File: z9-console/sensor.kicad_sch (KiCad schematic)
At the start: 17 parts, among them Q1 AO3400A, U4 ST_SENSOR_2, U5 IIS3DHHCTR

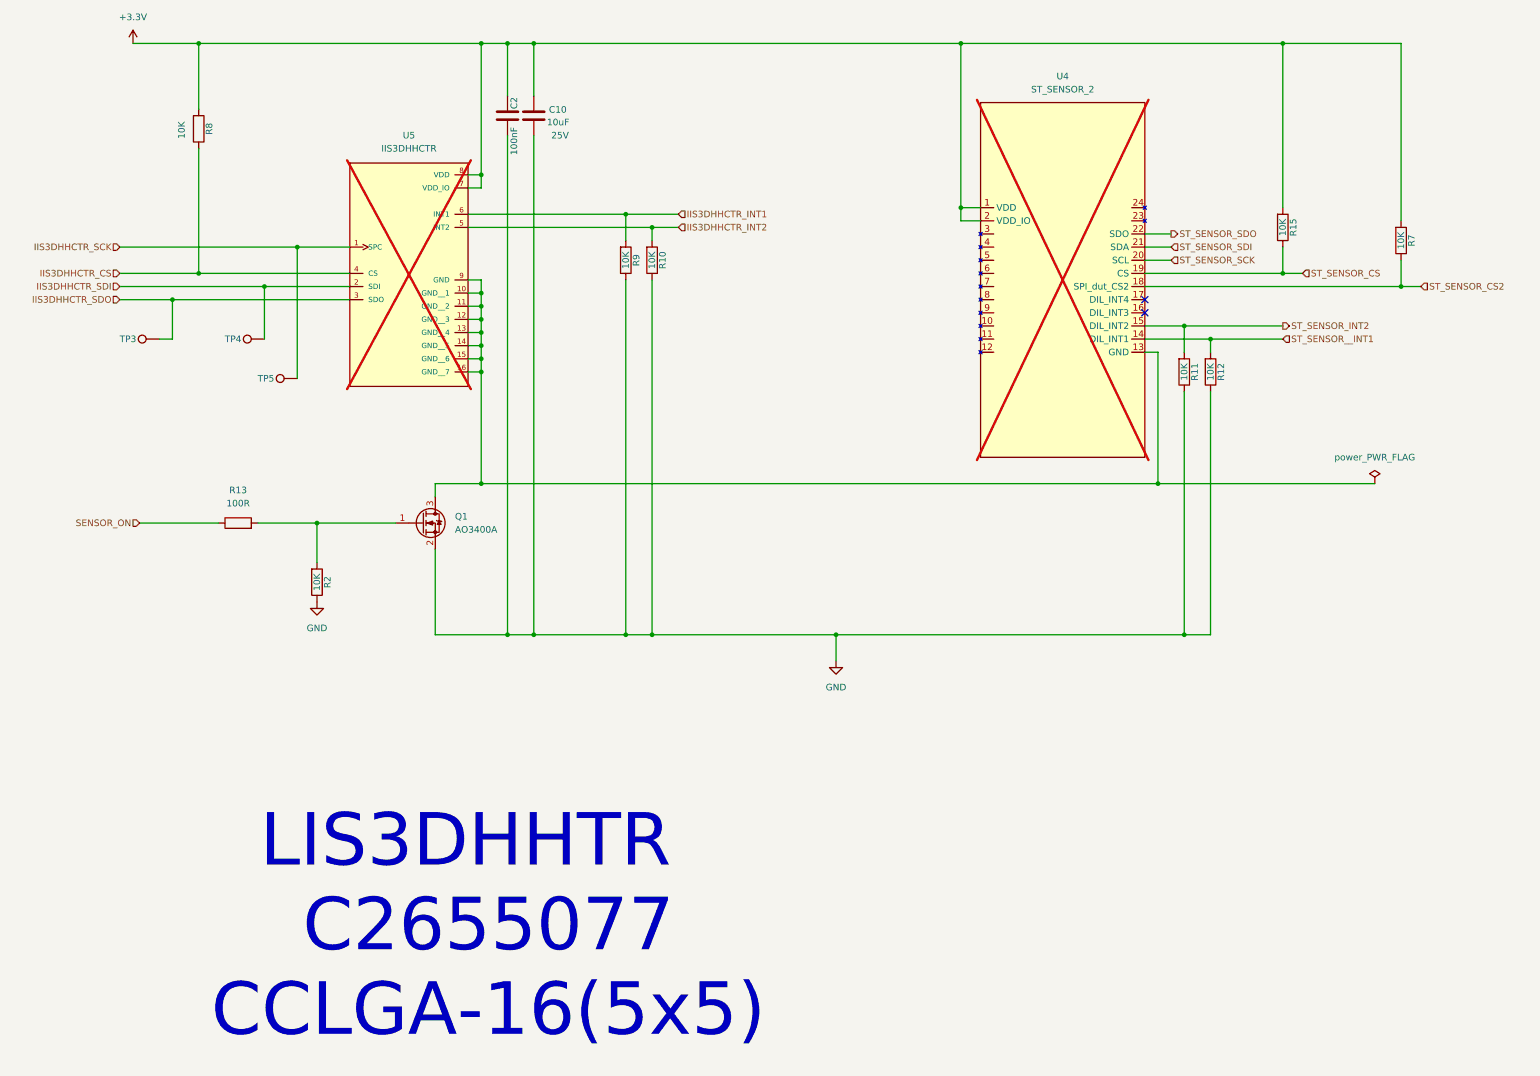
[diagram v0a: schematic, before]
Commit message: lcd power switch-- add new accelerometer
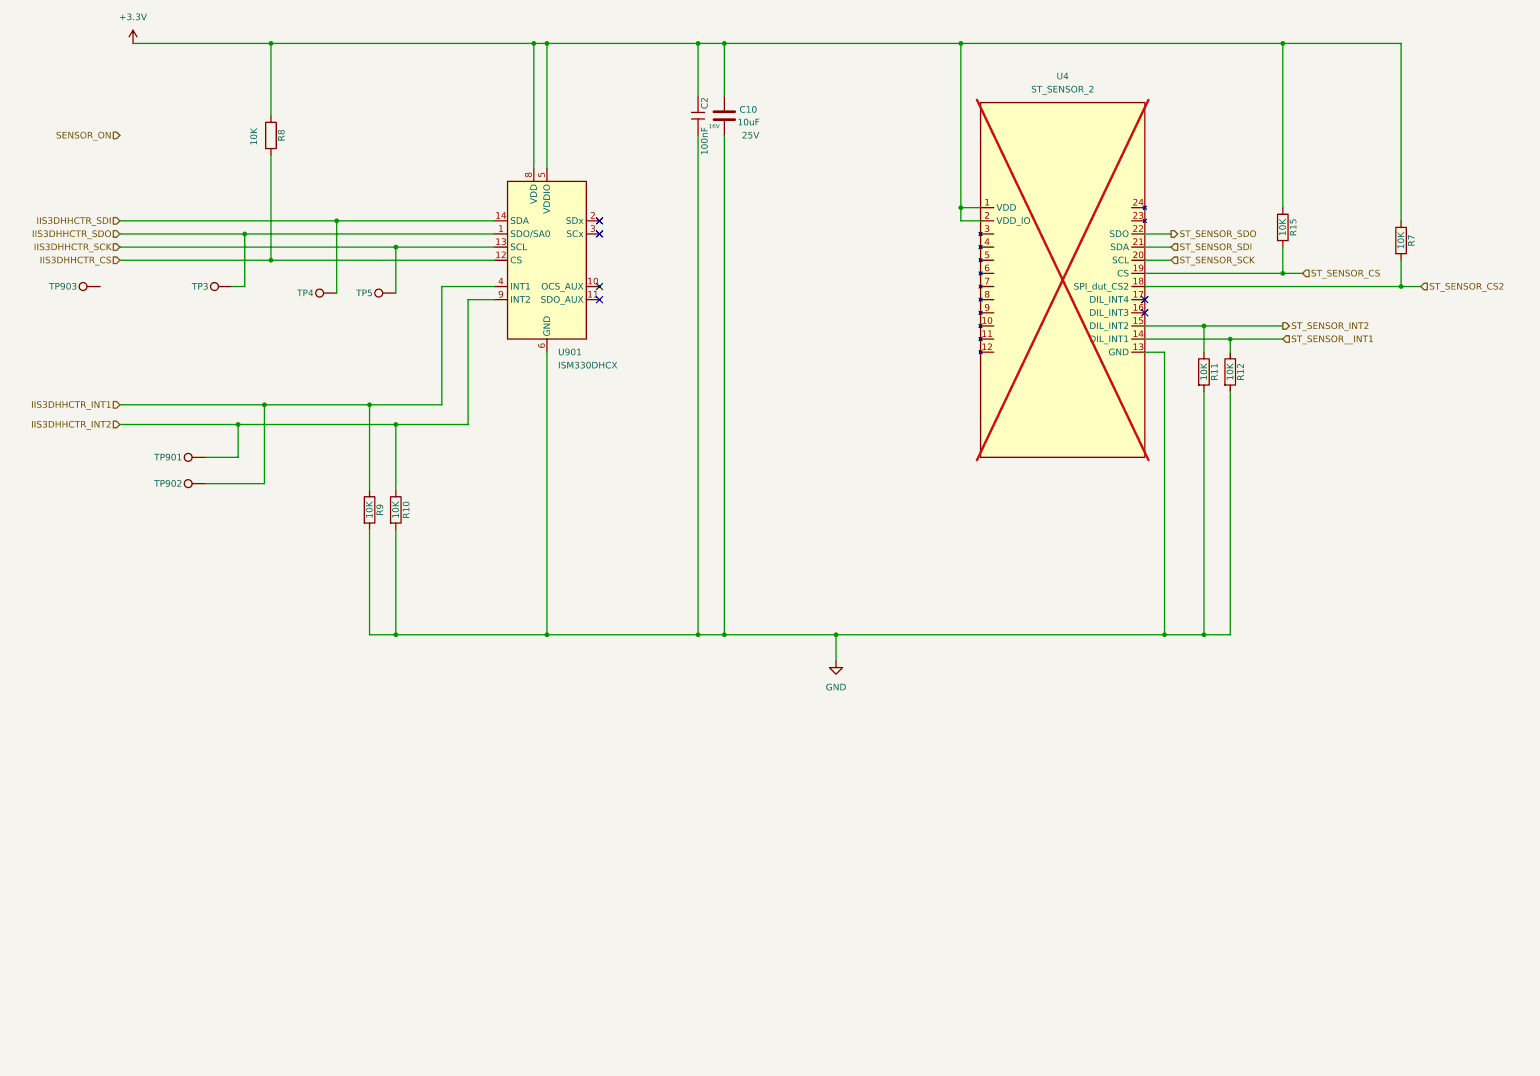
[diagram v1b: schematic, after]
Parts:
- removed Q1: AO3400A, Package_TO_SOT_SMD:SOT-23, symbol dnt_global:AO3400A
- removed R13: 100R, Resistor_SMD:R_0603_1608Metric, symbol Device:R
- removed R2: 10K, Resistor_SMD:R_0603_1608Metric, symbol Device:R
- removed U5: IIS3DHHCTR, dnt:CCLGA-16L_5X5X1P7_STM, symbol dnt_global:IIS3DHHCTR
- added TP901, TP902, TP903: IIS3DHHCTR_SDI, dnt:TestPoint_Pad_D1.0mm FP .6R, symbol Connector:TestPoint
- added U901: ISM330DHCX, Package_LGA:LGA-14_3x2.5mm_P0.5mm_LayoutBorder3x4y, symbol dnt_global:ISM330DHCX
- C2: footprint Capacitor_SMD:C_0603_1608Metric -> PCM_JLCPCB:C_0402; symbol Device:C -> dnt_global:0402,100nF, 16V; Attrition Qty (none) -> 10; Capacitance (none) -> 100nF; Category (none) -> Capacitors,Multilayer Ceramic Capacitors MLCC - SMD/SMT; Class (none) -> Basic Component; LCSC C14663 -> C1525; Manufacturer (none) -> Samsung Electro-Mechanics; Minimum Qty (none) -> 20; Part (none) -> CL05B104KO5NNNC; Price (none) -> 0.004USD; Process (none) -> SMT; Stock (none) -> 20208285; Temperature Coefficient (none) -> X7R; Tolerance (none) -> ±10%; Voltage Rated (none) -> 16V
- R10, R9: footprint Resistor_SMD:R_0603_1608Metric -> PCM_JLCPCB:R_0402; symbol Device:R -> dnt_global:Resistor_0402,10kΩ; Attrition Qty (none) -> 10; Category (none) -> Resistors,Chip Resistor - Surface Mount; Class (none) -> Basic Component; LCSC C25804 -> C25744; Manufacturer StackPole -> UNI-ROYAL(Uniroyal Elec); Minimum Qty (none) -> 20; Operating Temperature Range (none) -> -55°C~+155°C; Overload Voltage (Max) (none) -> 50V; Part (none) -> 0402WGF1002TCE; Part # RMCF0603JT10K0 -> (none); Power(Watts) (none) -> 62.5mW; Price (none) -> 0.004USD; Process (none) -> SMT; Resistance (none) -> 10kΩ; Stock (none) -> 24372091; Temperature Coefficient (none) -> ±100ppm/°C; Tolerance (none) -> ±1%; Type (none) -> Thick Film Resistors; VEND DIGI -> (none); VEND# RMCF0603JT10K0CT-ND -> (none)
- R11, R12, R15, R7, R8: footprint Resistor_SMD:R_0603_1608Metric -> PCM_JLCPCB:R_0402; symbol Device:R -> dnt_global:Resistor_0402,10kΩ; Attrition Qty (none) -> 10; Category (none) -> Resistors,Chip Resistor - Surface Mount; Class (none) -> Basic Component; LCSC C25804 -> C25744; Manufacturer (none) -> UNI-ROYAL(Uniroyal Elec); Minimum Qty (none) -> 20; Operating Temperature Range (none) -> -55°C~+155°C; Overload Voltage (Max) (none) -> 50V; Part (none) -> 0402WGF1002TCE; Power(Watts) (none) -> 62.5mW; Price (none) -> 0.004USD; Process (none) -> SMT; Resistance (none) -> 10kΩ; Stock (none) -> 24372091; Temperature Coefficient (none) -> ±100ppm/°C; Tolerance (none) -> ±1%; Type (none) -> Thick Film Resistors
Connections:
- net +3.3V: now also U901.5 (VDDIO), U901.8 (VDD)
- net GND: now also U4.13 (GND), U901.6 (GND), U901.7 (GND)
- net IIS3DHHCTR_CS: now also U901.12 (CS)
- net IIS3DHHCTR_INT1: now also TP902.1, U901.4 (INT1)
- net IIS3DHHCTR_INT2: now also TP901.1, U901.9 (INT2)
- net IIS3DHHCTR_SCK: now also U901.13 (SCL)
- net IIS3DHHCTR_SDI: now also U901.14 (SDA)
- net IIS3DHHCTR_SDO: now also U901.1 (SDO/SA0)
- no-connect marks 2 -> 6
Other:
- note removed: "LIS3DHHTR C2655077 CCLGA-16(5x5)"
- moved on the sheet: C10, C2, R10, R11, R12, R8, R9, TP3, TP4, TP5

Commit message: change MEMS device
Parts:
- renumbered C2 to C28, C10 to C29, R8 to R21, R9 to R22, R10 to R23, R11 to R24, R12 to R25, R15 to R26, R7 to R27, TP903 to TP37, TP901 to TP38, TP902 to TP39, TP3 to TP40, TP4 to TP41, TP5 to TP42, U901 to U10, U4 to U11
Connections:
- net IIS3DHHCTR_CS: now also TP37.1
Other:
- moved on the sheet: TP37, TP41, TP42

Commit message: final lcsc mappings
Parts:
- U10: LCSC (none) -> C2655101
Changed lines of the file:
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@@
 	(wire
 		(pts
-			(xy 245.11 78.74) (xy 260.35 78.74)
+			(xy 245.11 78.74) (xy 287.02 78.74)
 		)
 		(stroke
@@
 	(wire
 		(pts
-			(xy 260.35 68.58) (xy 264.16 68.58)
+			(xy 260.35 68.58) (xy 287.02 68.58)
 		)
 		(stroke
@@
 	(wire
 		(pts
-			(xy 250.19 81.28) (xy 260.35 81.28)
+			(xy 250.19 81.28) (xy 287.02 81.28)
 		)
 		(stroke
@@
 	(hierarchical_label "ST_SENSOR_CS"
 		(shape input)
-		(at 264.16 68.58 0)
+		(at 287.02 68.58 0)
 		(effects
 			(font
@@
 	(hierarchical_label "ST_SENSOR_INT2"
 		(shape output)
-		(at 260.35 78.74 0)
+		(at 287.02 78.74 0)
 		(effects
 			(font
@@
 	(hierarchical_label "ST_SENSOR__INT1"
 		(shape input)
-		(at 260.35 81.28 0)
+		(at 287.02 81.28 0)
 		(effects
 			(font
@@
 			(effects
 				(font
+					(size 1.27 1.27)
+				)
+				(hide yes)
+			)
+		)
+		(property "LCSC" " C2655101"
+			(at 118.11 66.04 0)
+			(effects
+				(font

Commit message: fix stdc - reroute power on pcb
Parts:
- TP37: value IIS3DHHCTR_SDI -> ISM_CS
- TP38: value IIS3DHHCTR_SDI -> ISM_INT1
- TP39: value IIS3DHHCTR_SDI -> ISM_INT2
- TP40: value IIS3DHHCTR_SDI -> ISM_SDO
- TP41: value IIS3DHHCTR_SDI -> ISM_SDI
- TP42: value IIS3DHHCTR_SCK -> ISM3_SCK
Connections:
- net +3.3V: now also U10.11 (SDO_AUX), U10.2 (SDx), U10.3 (SCx)
- net IIS3DHHCTR_CS renamed ISM_CS
- net IIS3DHHCTR_INT1 renamed ISM_INT1
- net IIS3DHHCTR_INT2 renamed ISM_INT2
- net IIS3DHHCTR_SCK renamed ISM_SCK
- net IIS3DHHCTR_SDI renamed ISM_SDI
- net IIS3DHHCTR_SDO renamed ISM_SDO
- no-connect marks 6 -> 3
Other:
- moved on the sheet: TP40
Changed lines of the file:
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@@
 	(paper "A3")
 	(junction
+		(at 132.08 58.42)
+		(diameter 0)
+		(color 0 0 0 0)
+	)
+	(junction
 		(at 147.32 138.43)
 		(diameter 0)
@@
 	)
 	(junction
+		(at 132.08 24.13)
+		(diameter 0)
+		(color 0 0 0 0)
+	)
+	(junction
 		(at 115.57 24.13)
 		(diameter 0)
@@
 	)
 	(junction
+		(at 132.08 60.96)
+		(diameter 0)
+		(color 0 0 0 0)
+	)
+	(junction
 		(at 198.12 55.88)
 		(diameter 0)
@@
 	)
 	(no_connect
-		(at 128.27 73.66)
-	)
-	(no_connect
-		(at 128.27 60.96)
-	)
-	(no_connect
-		(at 128.27 58.42)
-	)
-	(no_connect
 		(at 233.68 73.66)
 	)
@@
 	(wire
 		(pts
+			(xy 132.08 24.13) (xy 147.32 24.13)
+		)
+		(stroke
+			(width 0)
+			(type default)
+		)
+	)
+	(wire
+		(pts
 			(xy 260.35 24.13) (xy 283.21 24.13)
 		)
@@
 	(wire
 		(pts
+			(xy 128.27 58.42) (xy 132.08 58.42)
+		)
+		(stroke
+			(width 0)
+			(type default)
+		)
+	)
+	(wire
+		(pts
 			(xy 97.79 71.12) (xy 97.79 93.98)
 		)
@@
 	(wire
 		(pts
-			(xy 59.69 71.12) (xy 59.69 60.96)
+			(xy 59.69 72.39) (xy 59.69 60.96)
 		)
 		(stroke
@@
 	(wire
 		(pts
+			(xy 132.08 60.96) (xy 132.08 58.42)
+		)
+		(stroke
+			(width 0)
+			(type default)
+		)
+	)
+	(wire
+		(pts
 			(xy 63.5 109.22) (xy 63.5 93.98)
 		)
@@
 	(wire
 		(pts
-			(xy 57.15 71.12) (xy 59.69 71.12)
+			(xy 58.42 72.39) (xy 59.69 72.39)
 		)
 		(stroke
@@
 	(wire
 		(pts
+			(xy 128.27 60.96) (xy 132.08 60.96)
+		)
+		(stroke
+			(width 0)
+			(type default)
+		)
+	)
+	(wire
+		(pts
+			(xy 128.27 73.66) (xy 132.08 73.66)
+		)
+		(stroke
+			(width 0)
+			(type default)
+		)
+	)
+	(wire
+		(pts
 			(xy 233.68 78.74) (xy 245.11 78.74)
 		)
@@
 	(wire
 		(pts
-			(xy 118.11 24.13) (xy 147.32 24.13)
+			(xy 118.11 24.13) (xy 132.08 24.13)
 		)
 		(stroke
@@
 	(wire
 		(pts
+			(xy 132.08 58.42) (xy 132.08 24.13)
+		)
+		(stroke
+			(width 0)
+			(type default)
+		)
+	)
+	(wire
+		(pts
 			(xy 173.99 138.43) (xy 237.49 138.43)
 		)
@@
 	(wire
 		(pts
+			(xy 132.08 73.66) (xy 132.08 60.96)
+		)
+		(stroke
+			(width 0)
+			(type default)
+		)
+	)
+	(wire
+		(pts
 			(xy 152.4 24.13) (xy 198.12 24.13)
 		)
@@
 		)
 	)
-	(hierarchical_label "IIS3DHHCTR_SDO"
+	(hierarchical_label "ISM_SDO"
 		(shape input)
 		(at 35.56 60.96 180)
@@
 		)
 	)
-	(hierarchical_label "IIS3DHHCTR_INT1"
+	(hierarchical_label "ISM_INT1"
 		(shape input)
 		(at 35.56 93.98 180)
@@
 		)
 	)
-	(hierarchical_label "IIS3DHHCTR_SCK"
+	(hierarchical_label "ISM_SCK"
 		(shape input)
 		(at 35.56 63.5 180)
@@
 		)
 	)
-	(hierarchical_label "IIS3DHHCTR_INT2"
+	(hierarchical_label "ISM_INT2"
 		(shape input)
 		(at 35.56 97.79 180)
@@
 		)
 	)
-	(hierarchical_label "IIS3DHHCTR_SDI"
+	(hierarchical_label "ISM_SDI"
 		(shape input)
 		(at 35.56 58.42 180)
@@
 		)
 	)
-	(hierarchical_label "IIS3DHHCTR_CS"
+	(hierarchical_label "ISM_CS"
 		(shape input)
 		(at 35.56 66.04 180)
@@
 			)
 		)
-		(property "Value" "IIS3DHHCTR_SDI"
+		(property "Value" "ISM_INT2"
 			(at 42.545 109.22 90)
 			(effects
@@
 				)
 				(justify left)
-				(hide yes)
 			)
 		)
@@
 		(dnp no)
 		(property "Reference" "TP37"
-			(at 80.645 72.39 90)
+			(at 82.804 70.358 90)
 			(effects
 				(font
@@
 			)
 		)
-		(property "Value" "IIS3DHHCTR_SDI"
-			(at 75.565 72.39 90)
+		(property "Value" "ISM_CS"
+			(at 82.55 74.676 90)
 			(effects
 				(font
@@
 				)
 				(justify left)
-				(hide yes)
 			)
 		)
@@
 	(symbol
 		(lib_id "Connector:TestPoint")
-		(at 57.15 71.12 90)
+		(at 58.42 72.39 90)
 		(unit 1)
 		(exclude_from_sim no)
@@
 		(dnp no)
 		(property "Reference" "TP40"
-			(at 52.705 71.12 90)
+			(at 57.404 70.612 90)
 			(effects
 				(font
@@
 			)
 		)
-		(property "Value" "IIS3DHHCTR_SDI"
-			(at 47.625 71.12 90)
+		(property "Value" "ISM_SDO"
+			(at 58.928 75.184 90)
 			(effects
 				(font
@@
 				)
 				(justify left)
-				(hide yes)
 			)
 		)
 		(property "Footprint" "dnt:TestPoint_Pad_D1.0mm FP .6R"
-			(at 57.15 66.04 0)
+			(at 58.42 67.31 0)
 			(effects
 				(font
@@
 		)
 		(property "Datasheet" "~"
-			(at 57.15 66.04 0)
+			(at 58.42 67.31 0)
 			(effects
 				(font
@@
 		)
 		(property "Description" "test point"
-			(at 57.15 71.12 0)
+			(at 58.42 72.39 0)
 			(effects
 				(font
@@
 		)
 		(property "Part #" "DNP"
-			(at 202.565 285.75 0)
+			(at 203.835 287.02 0)
 			(effects
 				(font
@@
 		)
 		(property "VEND" "DNP"
-			(at 202.565 285.75 0)
+			(at 203.835 287.02 0)
 			(effects
 				(font
@@
 		)
 		(property "VEND#" "DNP"
-			(at 202.565 285.75 0)
+			(at 203.835 287.02 0)
 			(effects
 				(font
@@
 		)
 		(property "Manufacturer" "DNP"
-			(at 202.565 285.75 0)
+			(at 203.835 287.02 0)
 			(effects
 				(font
@@
 		)
 		(property "Sim.Device" ""
-			(at 57.15 71.12 0)
+			(at 58.42 72.39 0)
 			(effects
 				(font
@@
 		)
 		(property "Sim.Pins" ""
-			(at 57.15 71.12 0)
+			(at 58.42 72.39 0)
 			(effects
 				(font
@@
 		)
 		(property "Silkscreen" ""
-			(at 57.15 71.12 0)
+			(at 58.42 72.39 0)
 			(effects
 				(font
@@
 		(dnp no)
 		(property "Reference" "TP42"
-			(at 66.675 72.39 90)
+			(at 69.596 70.612 90)
 			(effects
 				(font
@@
 			)
 		)
-		(property "Value" "IIS3DHHCTR_SCK"
-			(at 61.595 72.39 90)
+		(property "Value" "ISM3_SCK"
+			(at 72.136 74.93 90)
 			(effects
 				(font
@@
 				)
 				(justify left)
-				(hide yes)
 			)
 		)
@@
 			)
 		)
-		(property "Value" "IIS3DHHCTR_SDI"
+		(property "Value" "ISM_INT1"
 			(at 42.545 104.14 90)
 			(effects
@@
 				)
 				(justify left)
-				(hide yes)
 			)
 		)
@@
 		(dnp no)
 		(property "Reference" "TP41"
-			(at 43.815 72.39 90)
+			(at 45.974 70.612 90)
 			(effects
 				(font
@@
 			)
 		)
-		(property "Value" "IIS3DHHCTR_SDI"
-			(at 38.735 72.39 90)
+		(property "Value" "ISM_SDI"
+			(at 47.244 75.184 90)
 			(effects
 				(font
@@
 				)
 				(justify left)
-				(hide yes)
 			)
 		)

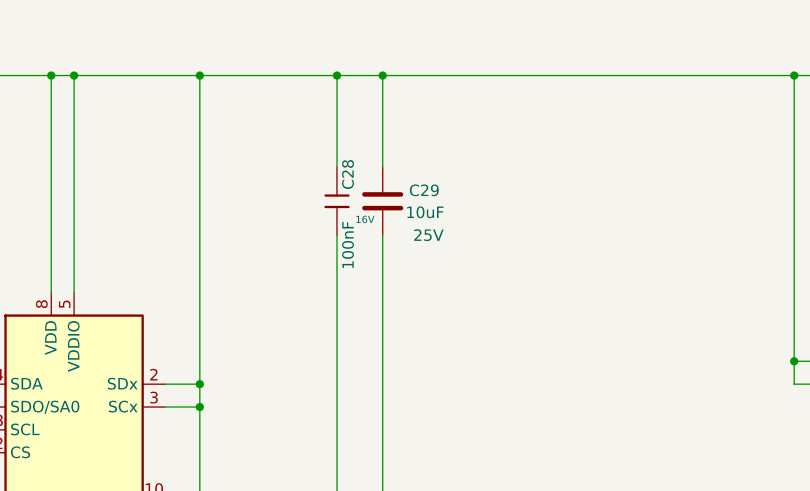
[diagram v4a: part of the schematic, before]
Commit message: fix 10uf 25v
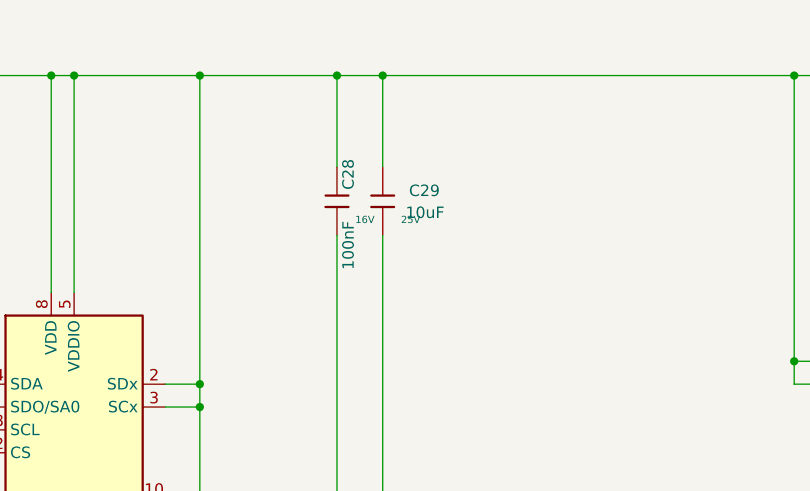
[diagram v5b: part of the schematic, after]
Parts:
- C29: footprint Capacitor_SMD:C_0603_1608Metric -> dnt:C_0603_1608Metric; symbol Device:C -> dnt_global:0603,10uF,_25V; Attrition Qty (none) -> 8; Capacitance (none) -> 10uF; Category (none) -> Capacitors,Multilayer Ceramic Capacitors MLCC - SMD/SMT; Class (none) -> Basic Component; Manufacturer (none) -> Samsung Electro-Mechanics; Minimum Qty (none) -> 20; Part (none) -> CL10A106MA8NRNC; Price (none) -> 0.021USD; Process (none) -> SMT; Stock (none) -> 3388297; Temperature Coefficient (none) -> X5R; Tolerance (none) -> ±20%; Voltage 25V -> (none); Voltage Rated (none) -> 25V
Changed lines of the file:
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@@
 	)
 	(symbol
-		(lib_id "Device:C")
+		(lib_id "dnt_global:0603,10uF,_25V")
 		(at 152.4 38.1 0)
 		(unit 1)
@@
 			)
 		)
-		(property "Footprint" "Capacitor_SMD:C_0603_1608Metric"
-			(at 153.3652 41.91 0)
+		(property "Footprint" "dnt:C_0603_1608Metric"
+			(at 150.622 38.1 90)
 			(effects
 				(font
@@
 			)
 		)
-		(property "Datasheet" "~"
+		(property "Datasheet" "https://www.lcsc.com/datasheet/lcsc_datasheet_2304140030_Samsung-Electro-Mechanics-CL10A106MA8NRNC_C96446.pdf"
 			(at 152.4 38.1 0)
 			(effects
@@
 			)
 		)
-		(property "Description" "Unpolarized capacitor"
-			(at 152.4 38.1 0)
-			(effects
-				(font
-					(size 1.27 1.27)
-				)
-				(hide yes)
-			)
-		)
-		(property "PN" ""
+		(property "Description" "25V 10uF X5R ±20% 0603 Multilayer Ceramic Capacitors MLCC - SMD/SMT ROHS"
 			(at 152.4 38.1 0)
 			(effects
@@
 			)
 		)
-		(property "Voltage" "25V"
-			(at 157.48 41.91 0)
-			(effects
-				(font
-					(size 1.27 1.27)
-				)
-			)
-		)
-		(property "Sim.Device" ""
+		(property "Stock" "3388297"
 			(at 152.4 38.1 0)
 			(effects
@@
 			)
 		)
-		(property "Sim.Pins" ""
+		(property "Price" "0.021USD"
 			(at 152.4 38.1 0)
 			(effects
@@
 			)
 		)
-		(property "Silkscreen" ""
+		(property "Process" "SMT"
 			(at 152.4 38.1 0)
 			(effects
+				(font
+					(size 1.27 1.27)
+				)
+				(hide yes)
+			)
+		)
+		(property "Minimum Qty" "20"
+			(at 152.4 38.1 0)
+			(effects
+				(font
+					(size 1.27 1.27)
+				)
+				(hide yes)
+			)
+		)
+		(property "Attrition Qty" "8"
+			(at 152.4 38.1 0)
+			(effects
+				(font
+					(size 1.27 1.27)
+				)
+				(hide yes)
+			)
+		)
+		(property "Class" "Basic Component"
+			(at 152.4 38.1 0)
+			(effects
+				(font
+					(size 1.27 1.27)
+				)
+				(hide yes)
+			)
+		)
+		(property "Category" "Capacitors,Multilayer Ceramic Capacitors MLCC - SMD/SMT"
+			(at 152.4 38.1 0)
+			(effects
+				(font
+					(size 1.27 1.27)
+				)
+				(hide yes)
+			)
+		)
+		(property "Manufacturer" "Samsung Electro-Mechanics"
+			(at 152.4 38.1 0)
+			(effects
+				(font
+					(size 1.27 1.27)
+				)
+				(hide yes)
+			)
+		)
+		(property "Part" "CL10A106MA8NRNC"
+			(at 152.4 38.1 0)
+			(effects
+				(font
+					(size 1.27 1.27)
+				)
+				(hide yes)
+			)
+		)
+		(property "Voltage Rated" "25V"
+			(at 154.432 40.1462 0)
+			(effects
+				(font
+					(size 0.8 0.8)
+				)
+				(justify left)
+			)
+		)
+		(property "Tolerance" "±20%"
+			(at 152.4 38.1 0)
+			(effects
+				(font
+					(size 1.27 1.27)
+				)
+				(hide yes)
+			)
+		)
+		(property "Capacitance" "10uF"
+			(at 152.4 38.1 0)
+			(effects
+				(font
+					(size 1.27 1.27)
+				)
+				(hide yes)
+			)
+		)
+		(property "Temperature Coefficient" "X5R"
+			(at 152.4 38.1 0)
+			(effects
